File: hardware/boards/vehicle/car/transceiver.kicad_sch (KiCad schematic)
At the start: 0 parts

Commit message: car schematic
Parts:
- added C25: 10nF, common:C_0603, symbol common:Capacitor
- added C26: 1nF, common:C_0603, symbol common:Capacitor
- added C27: 33nF, common:C_0603, symbol common:Capacitor
- added C28, C29: 22pF, common:C_0603, symbol common:Capacitor
- added C30: 2.2nF, common:C_0603, symbol common:Capacitor
- added C31: 4.7nF, common:C_0603, symbol common:Capacitor
- added C32, C37, C38, C39, C40: 1.5pF, common:C_0603, symbol common:Capacitor
- added C33: 1.0pF, common:C_0603, symbol common:Capacitor
- added C34: 220pF, common:C_0603, symbol common:Capacitor
- added C35: 1uF, common:C_0603, symbol common:Capacitor
- added C36: 0.3pF, common:C_0603, symbol common:Capacitor
- added J6: SMA, connector:SMA, symbol connector:SMA
- added L10, L9: 2.4nH, common:L_0603, symbol common:Inductor
- added L6: 8.2nH, common:L_0603, symbol common:Inductor
- added L7: 2.7nH, common:L_0603, symbol common:Inductor
- added L8: 3.9nH, common:L_0603, symbol common:Inductor
- added R24: 22k, common:R_0603, symbol common:Resistor
- added R26, R27: 1k, common:R_0603, symbol common:Resistor
- added R28: 20k, common:R_0603, symbol common:Resistor
- added U7: NRF24L01, transceiver:NRF24L01_QFN20, symbol transceiver:NRF24L01
- added U8: RFX2401C, transceiver:RFX2401C_QFN16, symbol transceiver:RFX2401C
- added Y3: 16MHz, common:Crystal_3225, symbol common:Crystal_4Pins
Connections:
- net CS: now also U7.2 (CSN)
- net EN: now also R27.1, U7.1 (CE)
- net MISO: now also U7.5 (MISO)
- net MOSI: now also U7.4 (MOSI)
- net SCK: now also U7.3 (SCK)
- new net: C30.1, C31.1, L7.2, R26.1, U7.11 (VDD_PA)
- new net: C29.2, U7.10 (XC1), Y3.3
- new net: L6.2, L7.1, U7.12 (ANT1)
- new net: L6.1, L8.1, U7.13 (ANT2)
- new net: R24.2, U7.16 (IREF)
- new net: C27.1, U7.19 (DVDD)
- new net: C28.2, U7.9 (XC2), Y3.1
- new net: R26.2, U8.5 (TXEN)
- new net: C32.2, C33.2, U8.4 (TXRX)
- new net: C32.1, L8.2
- new net: C38.2, C39.2, L10.1, L9.2
- new net: C36.2, C37.2, L9.1, U8.10 (ANT)
- new net: R27.2, R28.2, U8.6 (RXEN)
- new net: C40.2, J6.1 (ANT), L10.2
- new net 3V3: C25.2, C26.2, C34.1, C35.1, U7.15 (VDD), U7.18 (VDD), U7.7 (VDD), U8.16 (VDD)
- new net GND: C25.1, C26.1, C27.2, C28.1, C29.1, C30.2, C31.2, C33.1, C34.2, C35.2, C36.1, C37.1, C38.1, C39.1, C40.1, J6.2, J6.3, J6.4, J6.5, R24.1, R28.1, U7.14 (VSS), U7.17 (VSS), U7.20 (VSS), U7.8 (VSS), U8.1 (GND), U8.11 (GND), U8.12 (GND), U8.15 (GND), U8.17 (GND), U8.2 (GND), U8.3 (GND), U8.7 (GND), U8.8 (GND), U8.9 (GND), Y3.2 (GND), Y3.4 (GND)
- no-connect marks 0 -> 1

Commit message: added all footprints for lidar and car
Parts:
- added J7: 02x04, connector:Pin_02x04, symbol connector:Pin_02x04
- added R32: 1M, common:R_0603, symbol common:Resistor
- C28, C29: value 22pF -> 12pF
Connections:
- net 3V3: now also J7.8
- net CS: now also J7.7
- net EN: now also J7.2
- net GND: now also J7.1
- net MISO: now also J7.4
- net MOSI: now also J7.6
- net SCK: now also J7.3
- net at C29.2, U7.10 (XC1), Y3.3: now also R32.2
- net at C28.2, U7.9 (XC2), Y3.1: now also R32.1
- no-connect marks 1 -> 2
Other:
- moved on the sheet: C25, C26, C27, C28, C29, C30, C31, C32, C33, C34, C35, C36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

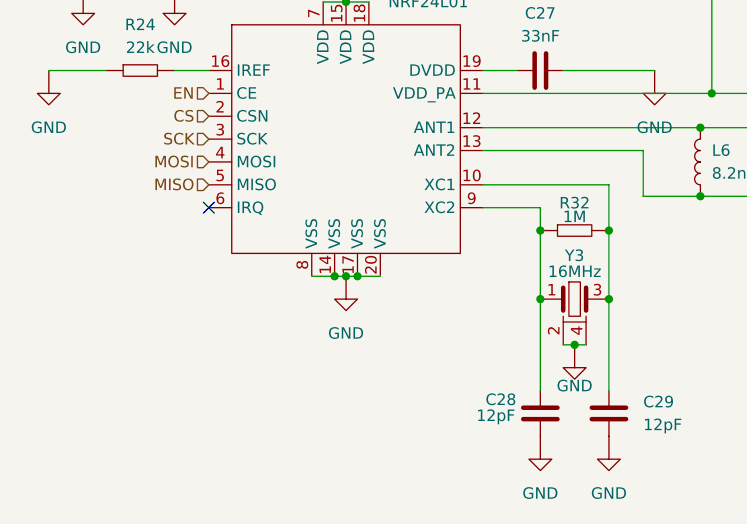
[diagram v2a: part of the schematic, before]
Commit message: corrected SD card and transceiver on symbol and schema
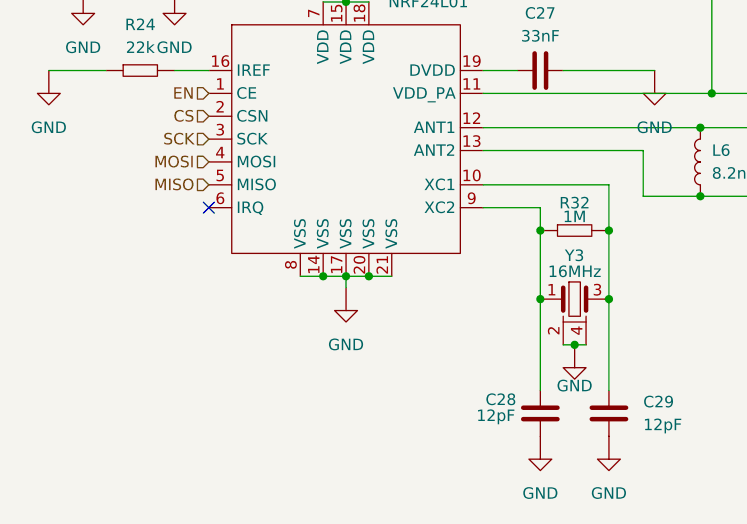
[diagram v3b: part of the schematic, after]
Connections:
- net GND: now also U7.21 (VSS)
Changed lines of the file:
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@@
-	)
-	(junction
-		(at 68.58 124.46)
-		(diameter 0)
-		(color 0 0 0 0)
 	)
 	(junction
@@
 	)
 	(junction
+		(at 67.31 124.46)
+		(diameter 0)
+		(color 0 0 0 0)
+	)
+	(junction
 		(at 233.68 109.22)
 		(diameter 0)
@@
 	)
 	(junction
-		(at 71.12 124.46)
-		(diameter 0)
-		(color 0 0 0 0)
-	)
-	(junction
 		(at 172.72 129.54)
 		(diameter 0)
@@
 	)
 	(junction
+		(at 69.85 124.46)
+		(diameter 0)
+		(color 0 0 0 0)
+	)
+	(junction
 		(at 171.45 129.54)
 		(diameter 0)
@@
 	)
 	(junction
-		(at 69.85 124.46)
-		(diameter 0)
-		(color 0 0 0 0)
-	)
-	(junction
 		(at 95.25 132.08)
+		(diameter 0)
+		(color 0 0 0 0)
+	)
+	(junction
+		(at 72.39 124.46)
 		(diameter 0)
 		(color 0 0 0 0)
@@
 	(wire
 		(pts
-			(xy 69.85 124.46) (xy 71.12 124.46)
-		)
-		(stroke
-			(width 0)
-			(type default)
-		)
-	)
-	(wire
-		(pts
 			(xy 184.15 124.46) (xy 184.15 129.54)
 		)
@@
 	(wire
 		(pts
-			(xy 66.04 124.46) (xy 68.58 124.46)
+			(xy 69.85 124.46) (xy 72.39 124.46)
 		)
 		(stroke
@@
 	(wire
 		(pts
-			(xy 71.12 124.46) (xy 73.66 124.46)
-		)
-		(stroke
-			(width 0)
-			(type default)
-		)
-	)
-	(wire
-		(pts
 			(xy 85.09 104.14) (xy 110.49 104.14)
 		)
@@
 	(wire
 		(pts
+			(xy 67.31 124.46) (xy 69.85 124.46)
+		)
+		(stroke
+			(width 0)
+			(type default)
+		)
+	)
+	(wire
+		(pts
 			(xy 67.31 93.98) (xy 69.85 93.98)
 		)
@@
 	(wire
 		(pts
+			(xy 64.77 124.46) (xy 67.31 124.46)
+		)
+		(stroke
+			(width 0)
+			(type default)
+		)
+	)
+	(wire
+		(pts
 			(xy 50.8 87.63) (xy 69.85 87.63)
 		)
@@
 	(wire
 		(pts
+			(xy 72.39 124.46) (xy 74.93 124.46)
+		)
+		(stroke
+			(width 0)
+			(type default)
+		)
+	)
+	(wire
+		(pts
 			(xy 163.83 129.54) (xy 166.37 129.54)
 		)
@@
 	(wire
 		(pts
+			(xy 69.85 124.46) (xy 69.85 125.73)
+		)
+		(stroke
+			(width 0)
+			(type default)
+		)
+	)
+	(wire
+		(pts
 			(xy 85.09 114.3) (xy 99.06 114.3)
 		)
@@
 		(pts
 			(xy 143.51 106.68) (xy 143.51 101.6)
-		)
-		(stroke
-			(width 0)
-			(type default)
-		)
-	)
-	(wire
-		(pts
-			(xy 68.58 124.46) (xy 69.85 124.46)
 		)
 		(stroke
@@
 	(symbol
 		(lib_id "pwr:GND")
-		(at 69.85 127 0)
+		(at 69.85 128.27 0)
 		(unit 1)
 		(exclude_from_sim no)
@@
 		(fields_autoplaced yes)
 		(property "Reference" "#GND054"
-			(at 69.85 114 0)
+			(at 69.85 115.27 0)
 			(effects
 				(font
@@
 		)
 		(property "Value" "GND"
-			(at 69.85 130.81 0)
+			(at 69.85 132.08 0)
 			(effects
 				(font
@@
 		)
 		(property "Footprint" ""
-			(at 69.85 127 0)
+			(at 69.85 128.27 0)
 			(effects
 				(font
@@
 		)
 		(property "Datasheet" ""
-			(at 69.85 127 0)
+			(at 69.85 128.27 0)
 			(effects
 				(font
@@
 		)
 		(property "Description" "Ground"
-			(at 69.85 131.5 0)
+			(at 69.85 132.77 0)
 			(effects
 				(font
@@
 		(pin "9"
 		)
+		(pin "21"
+		)
 		(instances
